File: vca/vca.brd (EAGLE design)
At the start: 33 x 107.6 mm, 36 parts, among them IC1 OPA4130U, IC2 OPA134D, IC3 OPA2134D, X1 2516-

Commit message: almost got the vca pcb done
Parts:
- added C2, C3, C4, C5, C6, C7: 10n, dan:C0603
- added R23, R24: 10, dan:R0603
- moved R2 36.7 mm to (20.3, 50.8), turned to 90 degrees
- moved R1 16.9 mm to (10.2, 76.2), turned to 90 degrees
- moved R5 15.3 mm to (26.7, 19.1)
- moved R12 7.18 mm to (8.89, 53.3)
- moved R13 6.35 mm to (11.4, 53.3)
- moved R14 4.02 mm to (6.35, 47.0)
- moved R3 3.59 mm to (3.81, 68.6)
- moved R9 2.84 mm to (6.35, 69.8)
- moved IC2 2.54 mm to (5.08, 53.3)
- moved R4 2.54 mm to (26.7, 34.3)
- moved R17 1.27 mm to (27.9, 39.4), turned to 90 degrees
- moved R18 1.27 mm to (25.4, 39.4), turned to 90 degrees
- moved RESP 1.27 mm to (26.7, 63.5)
- moved C1 1.27 mm to (30.5, 87.6)
- moved R21 1.27 mm to (27.9, 54.6)
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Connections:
- new net N$30: R23.2, X1.1, X1.2
- new net N$34: R24.2, X1.10, X1.9
- net +12V: now also C2.1, C3.1, C4.1, R24.1; no longer X1.10, X1.9
- net -12V: now also C5.1, C6.1, C7.1, R23.1; no longer X1.1, X1.2
- net GND: now also C2.2, C3.2, C4.2, C5.2, C6.2, C7.2, CVA.1; no longer CVA.3
- net N$26: now also CVA.3; no longer CVA.1
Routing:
- net +12V: track 0.00 -> 160.2 mm, vias 0 -> 12
- net -12V: track 0.00 -> 84.0 mm, vias 0 -> 6
- net N$1: track 0.00 -> 83.3 mm, vias 0 -> 6
- net N$4: track 0.00 -> 81.0 mm, vias 0 -> 4
- net N$18: track 0.00 -> 74.9 mm, vias 0 -> 4
- net N$13: track 0.00 -> 65.5 mm, vias 0 -> 2
- net N$7: track 5.40 -> 65.5 mm, vias 0 -> 4
- net N$14: track 0.00 -> 46.3 mm, vias 0 -> 3
- net N$9: track 0.00 -> 44.4 mm, vias 0 -> 4
- net NEG8: track 14.3 -> 56.4 mm, vias 0 -> 2
- net N$20: track 5.40 -> 47.3 mm
- net N$21: track 0.00 -> 40.9 mm, vias 0 -> 2
- net N$5: track 2.43 -> 43.3 mm, vias 0 -> 2
- net N$3: track 0.00 -> 37.4 mm
- net N$27: track 0.00 -> 31.3 mm, vias 0 -> 2
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- added copper zone on layer 16, net GND
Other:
- board size 33 x 107.6 mm -> 35.5 x 107.6 mm

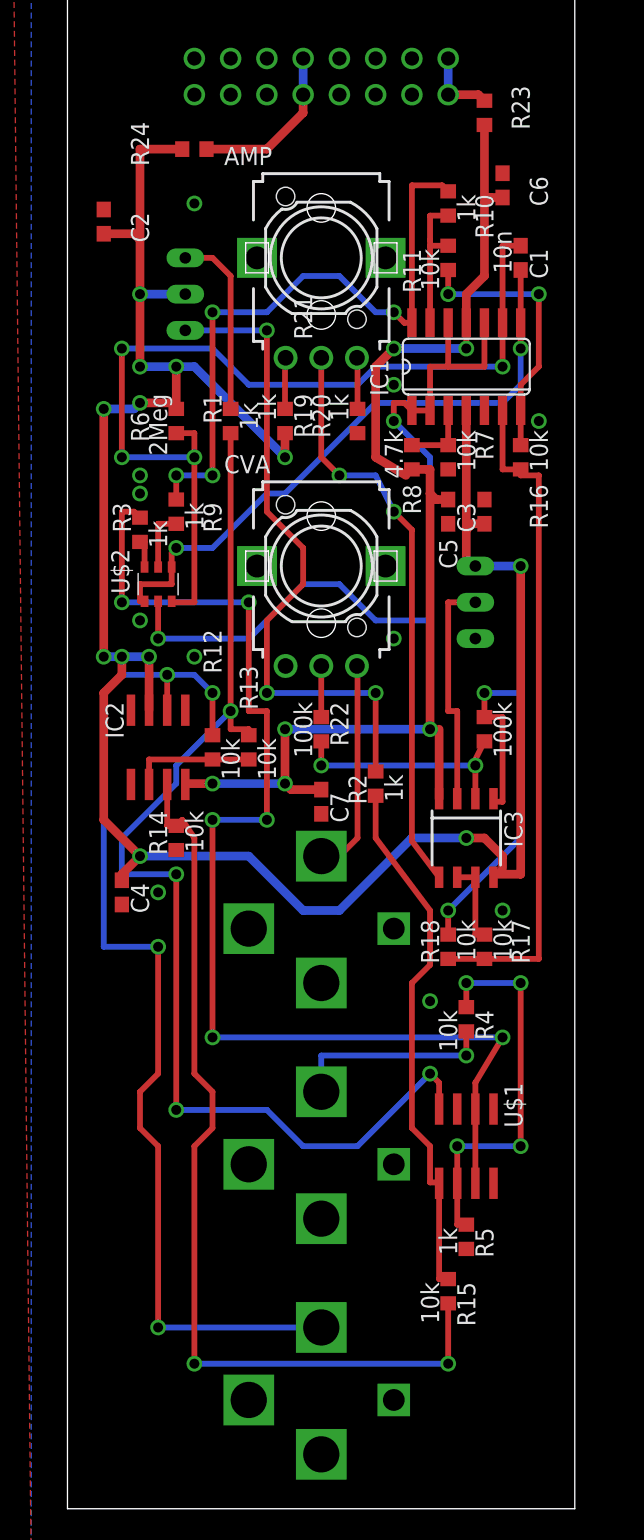
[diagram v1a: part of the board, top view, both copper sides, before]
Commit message: fixed bugs in vca.  did more changing of vcf components.  need to route a trace in vcf
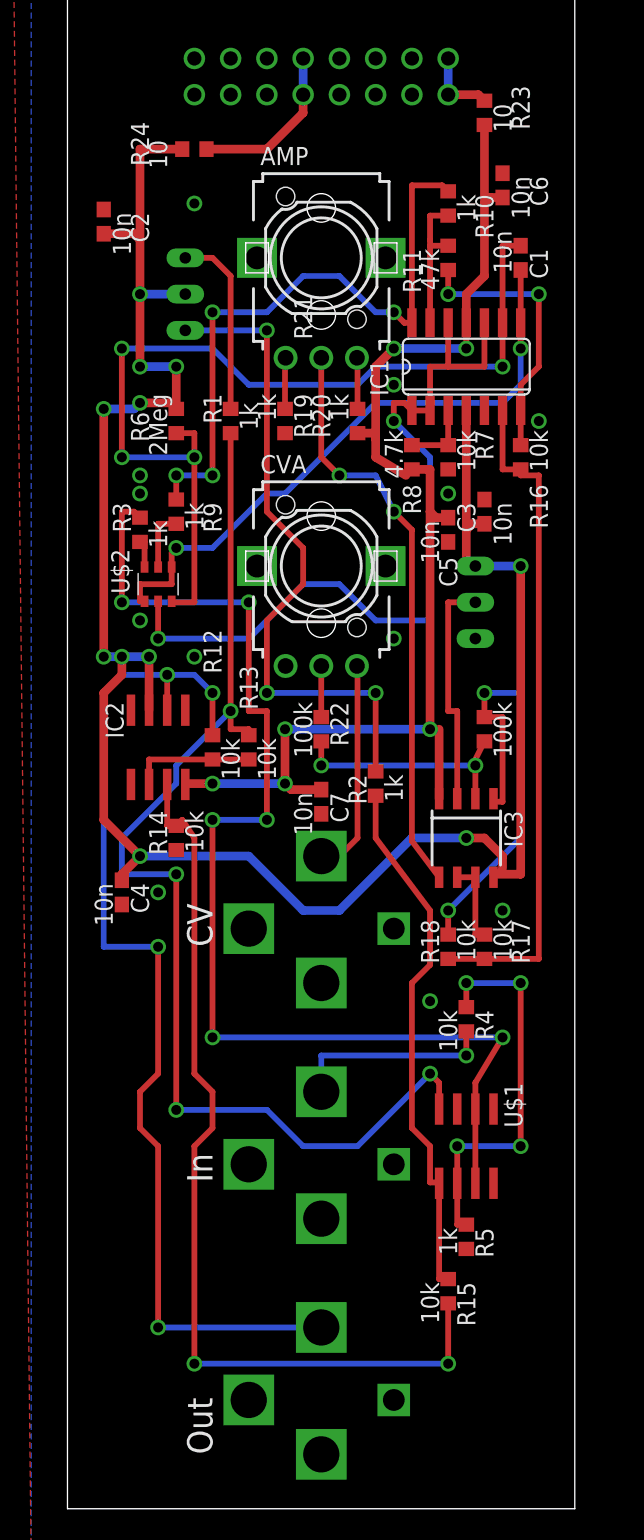
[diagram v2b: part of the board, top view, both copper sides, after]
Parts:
- R11: value 10k -> 47k
- moved C5 1.27 mm to (25.4, 68.6)
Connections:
- net +12V: no longer R19.1
- net -12V: now also R20.2
- net GND: now also R19.1; no longer R20.2
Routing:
- net +12V: track 160.2 -> 148.3 mm, vias 12 -> 11
- net -12V: track 84.0 -> 85.7 mm
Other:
- board text added: "CV"
- board text added: "In"
- board text added: "Out"
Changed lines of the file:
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@@
 <wire x1="34.27" y1="107.62" x2="-1.27" y2="107.62" width="0" layer="20"/>
 <wire x1="-1.27" y1="107.62" x2="-1.27" y2="0" width="0" layer="20"/>
+<text x="8.89" y="3.81" size="1.778" layer="21" font="vector" ratio="15" rot="R90">Out</text>
+<text x="8.89" y="22.86" size="1.778" layer="21" font="vector" ratio="15" rot="R90">In</text>
+<text x="8.89" y="39.37" size="1.778" layer="21" font="vector" ratio="15" rot="R90">CV</text>
 </plain>
 <attributes>
@@
 <elements>
 <element name="AMP" library="dan" package="EVUFXJ" value="US-EVUF2J" x="16.51" y="87.63" smashed="yes">
-<attribute name="NAME" x="9.7" y="94.13" size="1.27" layer="21" font="vector" ratio="15"/>
+<attribute name="NAME" x="12.24" y="94.13" size="1.27" layer="21" font="vector" ratio="15"/>
 </element>
 <element name="C1" library="dan" package="C0603" value="10n" x="30.48" y="87.63" smashed="yes" rot="R270">
@@
 </element>
 <element name="CVA" library="dan" package="EVUFXJ" value="US-EVUF2J" x="16.51" y="66.04" smashed="yes">
-<attribute name="NAME" x="9.7" y="72.54" size="1.27" layer="21" font="vector" ratio="15"/>
+<attribute name="NAME" x="12.24" y="72.54" size="1.27" layer="21" font="vector" ratio="15"/>
 </element>
 <element name="DCOS" library="dan" package="RJ9W" value="10k" x="6.35" y="85.09" smashed="yes" rot="MR90">
@@
 <attribute name="VALUE" x="26.035" y="92.075" size="1.27" layer="21" font="vector" ratio="15" rot="R270"/>
 </element>
-<element name="R11" library="dan" package="R0603" value="10k" x="25.4" y="87.63" smashed="yes" rot="R270">
+<element name="R11" library="dan" package="R0603" value="47k" x="25.4" y="87.63" smashed="yes" rot="R270">
 <attribute name="NAME" x="22.225" y="88.265" size="1.27" layer="21" font="vector" ratio="15" rot="R270"/>
 <attribute name="VALUE" x="23.495" y="88.265" size="1.27" layer="21" font="vector" ratio="15" rot="R270"/>
@@
 </element>
 <element name="C2" library="dan" package="C0603" value="10n" x="1.27" y="90.17" smashed="yes" rot="R90">
-<attribute name="NAME" x="3.175" y="90.805" size="1.27" layer="25" rot="R270"/>
-<attribute name="VALUE" x="1.905" y="90.805" size="1.27" layer="27" rot="R270"/>
+<attribute name="NAME" x="3.175" y="90.805" size="1.27" layer="21" font="vector" ratio="15" rot="R270"/>
+<attribute name="VALUE" x="1.905" y="90.805" size="1.27" layer="21" font="vector" ratio="15" rot="R270"/>
 </element>
 <element name="C3" library="dan" package="C0603" value="10n" x="27.94" y="69.85" smashed="yes" rot="R90">
-<attribute name="NAME" x="26.035" y="70.485" size="1.27" layer="25" rot="R270"/>
-<attribute name="VALUE" x="28.575" y="70.485" size="1.27" layer="27" rot="R270"/>
+<attribute name="NAME" x="26.035" y="70.485" size="1.27" layer="21" font="vector" ratio="15" rot="R270"/>
+<attribute name="VALUE" x="28.575" y="70.485" size="1.27" layer="21" font="vector" ratio="15" rot="R270"/>
 </element>
 <element name="C4" library="dan" package="C0603" value="10n" x="2.54" y="43.18" smashed="yes" rot="R270">
-<attribute name="NAME" x="3.175" y="43.815" size="1.27" layer="25" rot="R270"/>
-<attribute name="VALUE" x="0.635" y="43.815" size="1.27" layer="27" rot="R270"/>
-</element>
-<element name="C5" library="dan" package="C0603" value="10n" x="25.4" y="69.85" smashed="yes" rot="R270">
-<attribute name="NAME" x="24.765" y="67.945" size="1.27" layer="25" rot="R270"/>
-<attribute name="VALUE" x="23.495" y="70.485" size="1.27" layer="27" rot="R270"/>
+<attribute name="NAME" x="3.175" y="43.815" size="1.27" layer="21" font="vector" ratio="15" rot="R270"/>
+<attribute name="VALUE" x="0.635" y="43.815" size="1.27" layer="21" font="vector" ratio="15" rot="R270"/>
+</element>
+<element name="C5" library="dan" package="C0603" value="10n" x="25.4" y="68.58" smashed="yes" rot="R270">
+<attribute name="NAME" x="24.765" y="66.675" size="1.27" layer="21" font="vector" ratio="15" rot="R270"/>
+<attribute name="VALUE" x="23.495" y="69.215" size="1.27" layer="21" font="vector" ratio="15" rot="R270"/>
 </element>
 <element name="C6" library="dan" package="C0603" value="10n" x="29.21" y="92.71" smashed="yes" rot="R90">
-<attribute name="NAME" x="31.115" y="93.345" size="1.27" layer="25" rot="R270"/>
-<attribute name="VALUE" x="29.845" y="93.345" size="1.27" layer="27" rot="R270"/>
+<attribute name="NAME" x="31.115" y="93.345" size="1.27" layer="21" font="vector" ratio="15" rot="R270"/>
+<attribute name="VALUE" x="29.845" y="93.345" size="1.27" layer="21" font="vector" ratio="15" rot="R270"/>
 </element>
 <element name="C7" library="dan" package="C0603" value="10n" x="16.51" y="49.53" smashed="yes" rot="R270">
-<attribute name="NAME" x="17.145" y="50.165" size="1.27" layer="25" rot="R270"/>
-<attribute name="VALUE" x="14.605" y="50.165" size="1.27" layer="27" rot="R270"/>
+<attribute name="NAME" x="17.145" y="50.165" size="1.27" layer="21" font="vector" ratio="15" rot="R270"/>
+<attribute name="VALUE" x="14.605" y="50.165" size="1.27" layer="21" font="vector" ratio="15" rot="R270"/>
 </element>
 <element name="R23" library="dan" package="R0603" value="10" x="27.94" y="97.79" smashed="yes" rot="R90">
-<attribute name="NAME" x="29.845" y="99.695" size="1.27" layer="25" rot="R270"/>
-<attribute name="VALUE" x="28.575" y="98.425" size="1.27" layer="27" rot="R270"/>
+<attribute name="NAME" x="29.845" y="99.695" size="1.27" layer="21" font="vector" ratio="15" rot="R270"/>
+<attribute name="VALUE" x="28.575" y="98.425" size="1.27" layer="21" font="vector" ratio="15" rot="R270"/>
 </element>
 <element name="R24" library="dan" package="R0603" value="10" x="7.62" y="95.25" smashed="yes">
-<attribute name="NAME" x="3.175" y="97.155" size="1.27" layer="25" rot="R270"/>
-<attribute name="VALUE" x="4.445" y="95.885" size="1.27" layer="27" rot="R270"/>
+<attribute name="NAME" x="3.175" y="97.155" size="1.27" layer="21" font="vector" ratio="15" rot="R270"/>
+<attribute name="VALUE" x="4.445" y="95.885" size="1.27" layer="21" font="vector" ratio="15" rot="R270"/>
 </element>
 </elements>
@@
 <contactref element="OUT" pad="P$1"/>
 <contactref element="OUT" pad="P$4"/>
-<contactref element="R20" pad="2"/>
 <contactref element="RESP" pad="E"/>
 <contactref element="CVIN" pad="P$2"/>
@@
 <contactref element="C6" pad="2"/>
 <contactref element="C4" pad="2"/>
-<wire x1="25.4" y1="72.81" x2="27.94" y2="70.7" width="0" layer="19" extent="1-1"/>
+<via x="25.4" y="71.12" extent="1-16" drill="0.7"/>
+<contactref element="R19" pad="1"/>
 </signal>
 <signal name="N$6">
@@
 <contactref element="IC2" pad="7"/>
 <contactref element="IC3" pad="8"/>
-<contactref element="R19" pad="1"/>
 <contactref element="RESP" pad="A"/>
 <wire x1="27.305" y1="66.04" x2="26.67" y2="66.04" width="0.4064" layer="1"/>
@@
 <wire x1="6.35" y1="77.05" x2="6.35" y2="80.01" width="0.6096" layer="1"/>
 <via x="6.35" y="80.01" extent="1-16" drill="0.7"/>
-<wire x1="6.35" y1="80.01" x2="7.62" y2="80.01" width="0.6096" layer="16"/>
-<wire x1="7.62" y1="80.01" x2="13.97" y2="73.66" width="0.6096" layer="16"/>
-<via x="13.97" y="73.66" extent="1-16" drill="0.7"/>
-<wire x1="13.97" y1="73.66" x2="13.97" y2="75.35" width="0.6096" layer="1"/>
 <via x="1.27" y="77.05" extent="1-16" drill="0.7"/>
 <wire x1="1.27" y1="77.05" x2="3.39" y2="77.05" width="0.6096" layer="16"/>
@@
 <contactref element="IC3" pad="4"/>
 <wire x1="22.86" y1="72.81" x2="24.13" y2="72.81" width="0.6096" layer="1"/>
-<wire x1="24.13" y1="72.81" x2="24.13" y2="71.12" width="0.6096" layer="1"/>
-<wire x1="24.13" y1="71.12" x2="24.13" y2="54.61" width="0.6096" layer="1"/>
+<wire x1="24.13" y1="72.81" x2="24.13" y2="69.85" width="0.6096" layer="1"/>
+<wire x1="24.13" y1="69.85" x2="24.13" y2="54.61" width="0.6096" layer="1"/>
 <wire x1="24.13" y1="54.61" x2="24.765" y2="54.61" width="0.4064" layer="1"/>
 <wire x1="24.765" y1="54.61" x2="24.765" y2="49.74" width="0.6096" layer="1"/>
@@
 <via x="21.59" y="81.28" extent="1-16" drill="0.7"/>
 <wire x1="21.59" y1="81.28" x2="20.32" y2="80.01" width="0.6096" layer="1"/>
-<wire x1="20.32" y1="80.01" x2="20.32" y2="73.66" width="0.6096" layer="1"/>
+<wire x1="20.32" y1="80.01" x2="20.32" y2="74.93" width="0.6096" layer="1"/>
+<wire x1="20.32" y1="74.93" x2="20.32" y2="73.66" width="0.6096" layer="1"/>
 <wire x1="20.32" y1="73.66" x2="22.44" y2="72.39" width="0.6096" layer="1"/>
 <wire x1="22.44" y1="72.39" x2="22.86" y2="72.81" width="0.4064" layer="1"/>
@@
 <wire x1="29.21" y1="91.86" x2="28.36" y2="91.86" width="0.6096" layer="1"/>
 <wire x1="28.36" y1="91.86" x2="27.94" y2="91.44" width="0.6096" layer="1"/>
-<wire x1="25.4" y1="70.7" x2="24.55" y2="70.7" width="0.6096" layer="1"/>
-<wire x1="24.55" y1="70.7" x2="24.13" y2="71.12" width="0.6096" layer="1"/>
+<wire x1="25.4" y1="69.43" x2="24.55" y2="69.43" width="0.6096" layer="1"/>
+<wire x1="24.55" y1="69.43" x2="24.13" y2="69.85" width="0.6096" layer="1"/>
+<contactref element="R20" pad="2"/>
+<wire x1="19.05" y1="75.35" x2="20.32" y2="75.35" width="0.6096" layer="1"/>
+<wire x1="20.32" y1="75.35" x2="20.32" y2="74.93" width="0.4064" layer="1"/>
 </signal>
 <signal name="NEG8">
